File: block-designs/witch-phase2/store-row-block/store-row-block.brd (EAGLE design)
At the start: 27.9 x 27.9 mm, 15 parts, among them IC1 74LVC1G125DBV, Q1 MMBT2907ALT1SMD

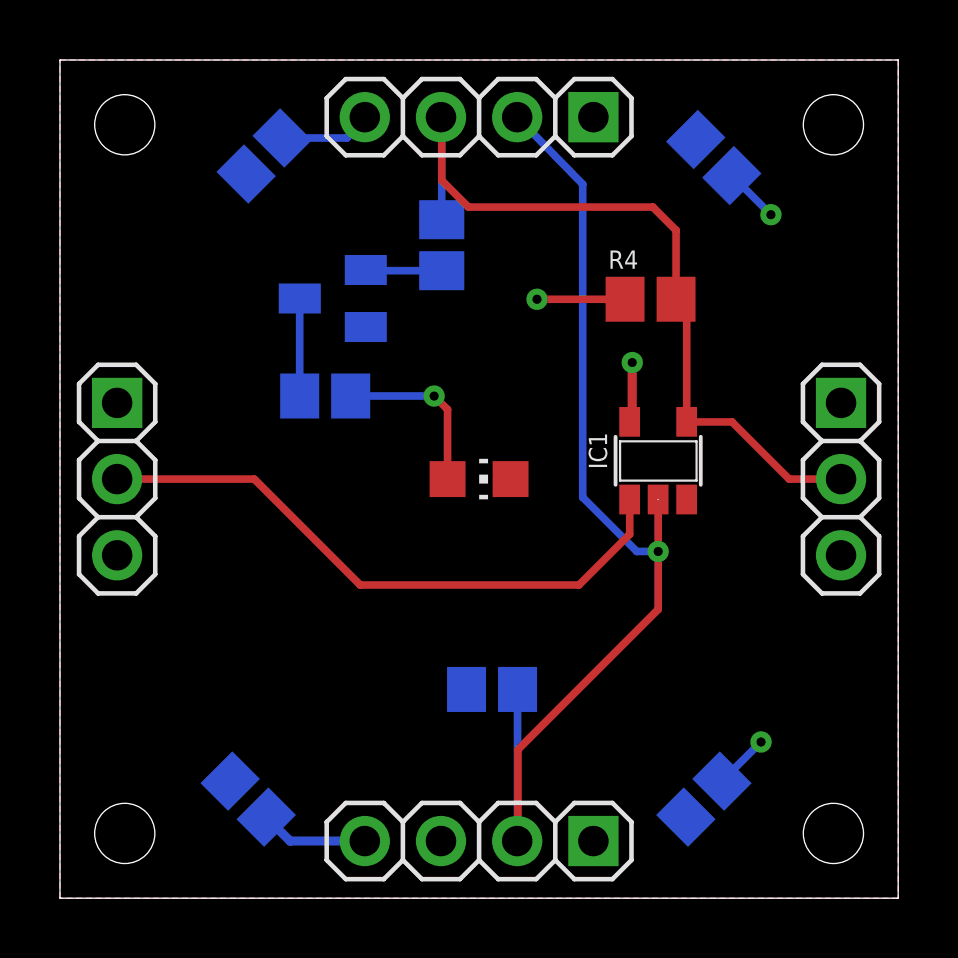
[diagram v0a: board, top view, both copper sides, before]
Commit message: updated board layout pictures and pdf schematics
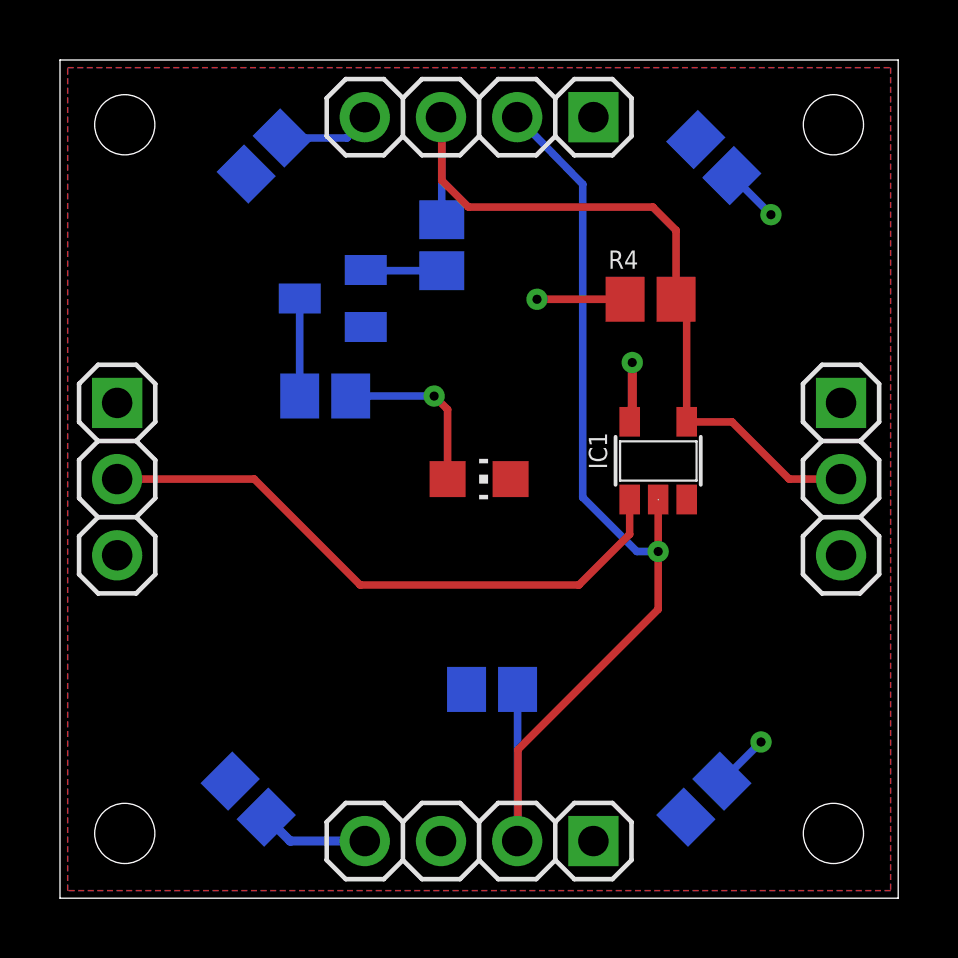
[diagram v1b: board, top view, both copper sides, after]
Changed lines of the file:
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@@
 <text x="5.7912" y="25.4508" size="1.016" layer="48">TOP</text>
 <text x="19.3802" y="25.5016" size="1.016" layer="48">TOP</text>
-<text x="1.9304" y="6.0452" size="0.6096" layer="48">  ROW
+<text x="0.762" y="5.08" size="0.6096" layer="48">ROW
 SELECT</text>
 </plain>
@@
 <contactref element="JP2" pad="4"/>
 <contactref element="JP4" pad="4"/>
-<polygon width="0" layer="1">
-<vertex x="27.94" y="0"/>
-<vertex x="0" y="0"/>
-<vertex x="0" y="27.94"/>
-<vertex x="27.94" y="27.94"/>
+<polygon width="0.254" layer="1">
+<vertex x="27.686" y="0.254"/>
+<vertex x="0.254" y="0.254"/>
+<vertex x="0.254" y="27.686"/>
+<vertex x="27.686" y="27.686"/>
 </polygon>
 <contactref element="IC1" pad="3"/>
@@
 <contactref element="JP2" pad="1"/>
 <contactref element="JP4" pad="1"/>
-<polygon width="0" layer="16">
-<vertex x="27.94" y="0"/>
-<vertex x="0" y="0"/>
-<vertex x="0" y="27.94"/>
-<vertex x="27.94" y="27.94"/>
+<polygon width="0.254" layer="16">
+<vertex x="27.686" y="0.254"/>
+<vertex x="0.254" y="0.254"/>
+<vertex x="0.254" y="27.686"/>
+<vertex x="27.686" y="27.686"/>
 </polygon>
 <contactref element="IC1" pad="5"/>

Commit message: updated designs for new labeling and spacing
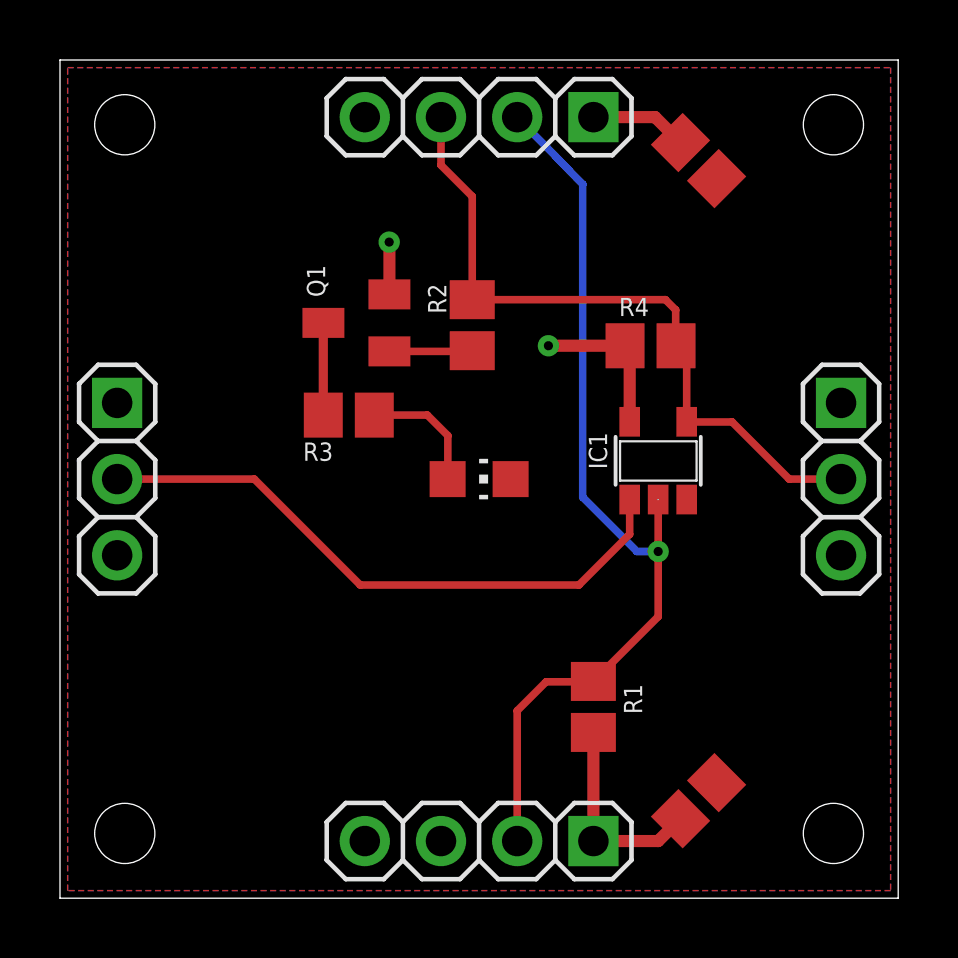
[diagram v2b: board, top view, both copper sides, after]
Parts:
- removed C2, C3: (no value), resistor:C0805
- moved R1 3.43 mm to (17.8, 6.38), flipped to the top, turned to 270 degrees
- moved R2 2.85 mm to (13.7, 19.1), flipped to the top
- moved R4 1.55 mm to (19.7, 18.4)
- moved Q1 1.13 mm to (9.88, 19.2), flipped to the top, turned to 90 degrees
- moved R3 1.01 mm to (9.63, 16.1), flipped to the top, turned to 0 degrees
- moved C4 0.52 mm to (21.3, 24.6), flipped to the top, turned to 315 degrees
- moved C1 0.18 mm to (21.3, 3.25), flipped to the top, turned to 45 degrees
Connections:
- removed net +5V: C1.1, C2.1, C3.1, C4.1, IC1.5, JP2.1, JP4.1, Q1.E, R1.2, R4.2
- new net VCC: C1.1, C4.1, IC1.5, JP2.1, JP4.1, Q1.E, R1.2, R4.2
- net GND: no longer C2.2, C3.2
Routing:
- net VCC: track 0.00 -> 17.0 mm, vias 0 -> 2
- net GND: track 10.4 -> 0.00 mm, vias 2 -> 0
- net +5V: track 4.95 -> 0.00 mm, vias 2 -> 0
- net SND_RCV: track 35.2 -> 31.1 mm
- net ROW_EN: track 27.0 -> 23.7 mm
- net N$5: track 5.74 -> 4.19 mm, vias 1 -> 0
- added copper zone on layer 16, net VCC
- removed copper zone on layer 16, net +5V
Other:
- board text added: "ROW SEL"
- board text removed: "ROW SELECT"
- board text removed: "TOP"
